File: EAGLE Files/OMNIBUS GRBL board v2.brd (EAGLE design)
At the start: 100.6 x 73.6 mm, 61 parts, among them K1 691131710002, K2 691131710003, K3 691131710003, K4 691131710003, U1 LTV-847S, U2 L7805ACD2T-TR, U3 LM358M/NOPB, U4 LTV-847S, U5 PC817X3NSZ1B, U6 ULN2003AD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

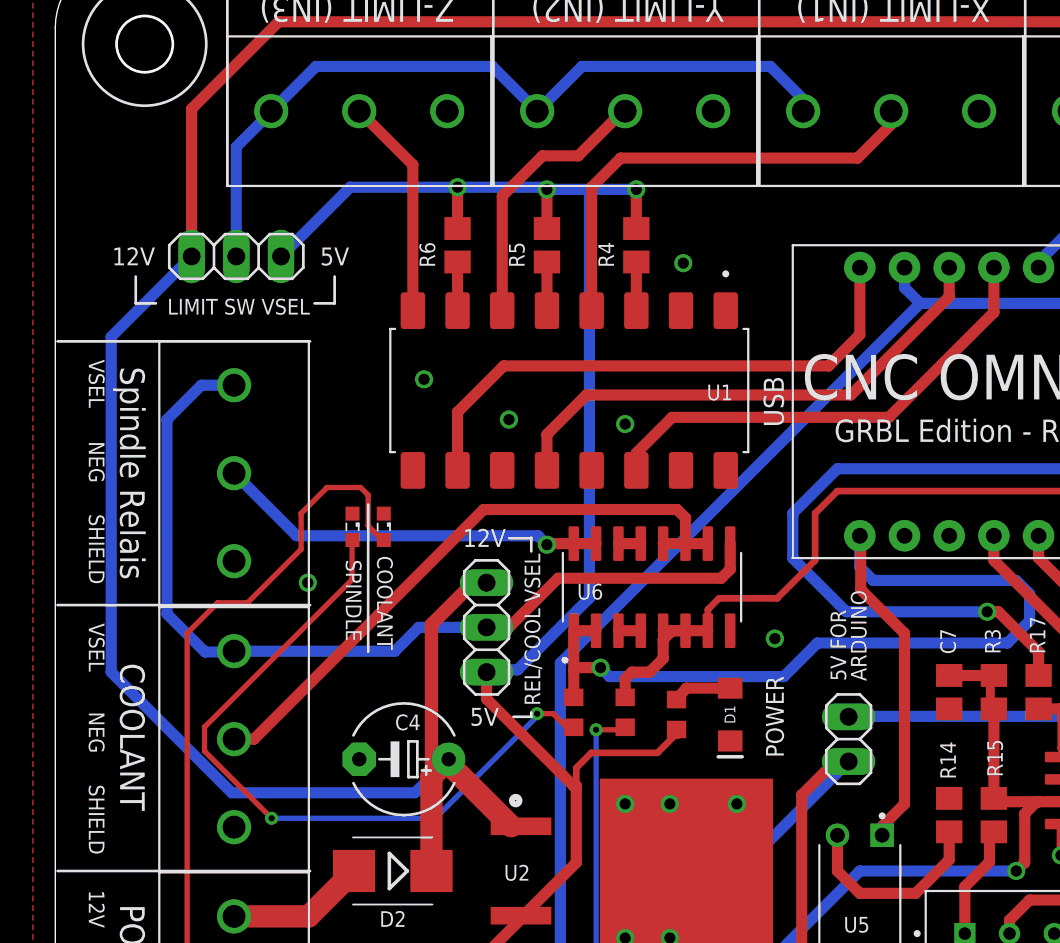
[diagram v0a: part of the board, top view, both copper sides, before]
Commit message: PCB Bugfixes and polishing
• DRV Shield had an routing error (laser indicator LED) also R3 had a wrong value
• New Footprint for the 0.33uF Caps
• Silkscreen polishing
• almost all LEDs are 0805 package now
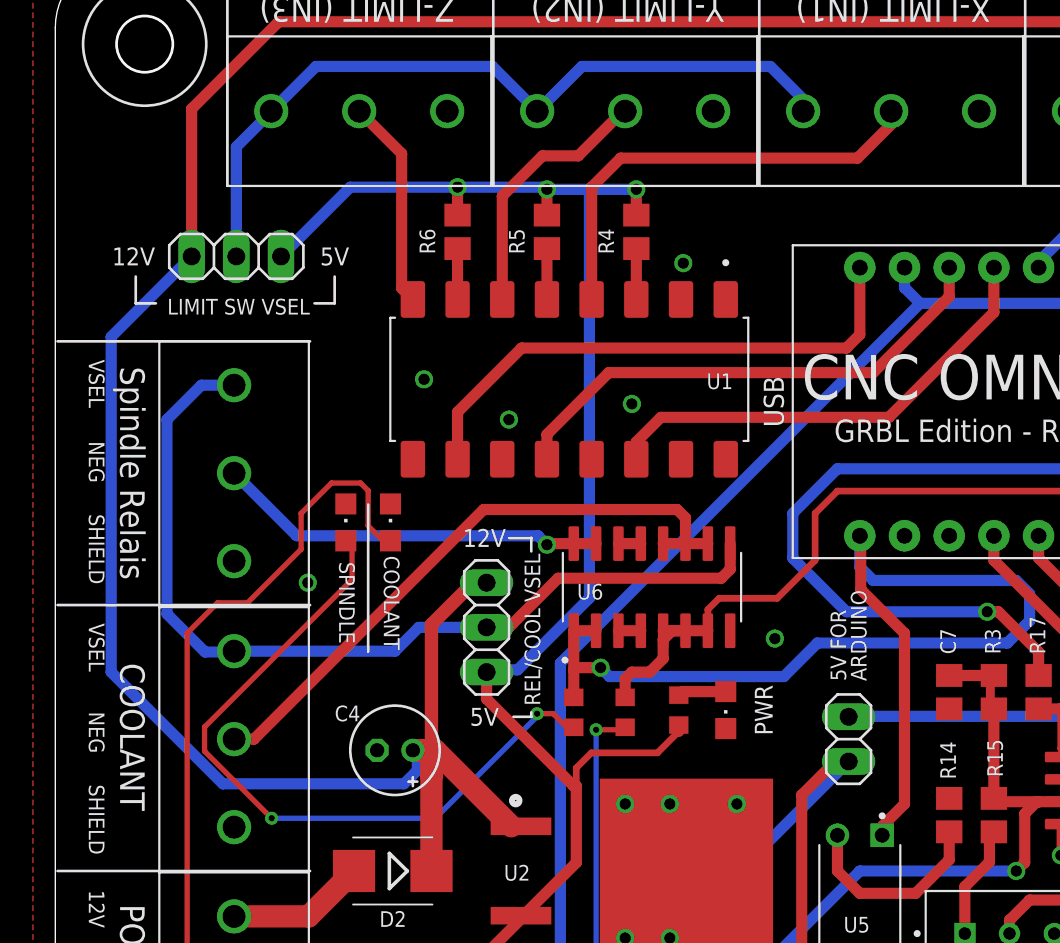
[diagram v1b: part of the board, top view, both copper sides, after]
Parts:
- removed D1: (no value), SparkFun-LED:LED-1206
- removed LED2, LED4: (no value), eagle-ltspice:LED_SML0603
- added GREEN, RED1, RED2: (no value), led:CHIPLED_0805
- C4: value 220uf -> 0.33uF 50V; device rcl:E5-6 -> rcl:E2-5
- moved R4 0.76 mm to (30.5, 56.6)
- moved R5 0.76 mm to (25.4, 56.6)
- moved R6 0.76 mm to (20.3, 56.6)
- moved C4 0.72 mm to (16.8, 27.2)
- moved U1 0.63 mm to (26.7, 48.3)
- moved R2 0.28 mm to (32.9, 29.5)
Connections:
- net GND: now also GREEN.C, RED1.C, RED2.C; no longer D1.C, LED2.C, LED4.C
- net N$1: now also GREEN.A; no longer D1.A
- net N$11: now also RED2.A; no longer LED2.A
- net N$12: now also RED1.A; no longer LED4.A
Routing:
- net 12V: track 255.3 -> 257.3 mm
- net 5V: track 255.9 -> 253.9 mm
- net N$12: track 81.5 -> 82.2 mm
- net INPUT3: track 12.6 -> 12.0 mm
- net INPUT2: track 15.5 -> 14.9 mm
- net INPUT1: track 26.3 -> 25.6 mm
- net IN3: track 31.8 -> 31.2 mm
- net IN2: track 29.8 -> 29.2 mm
- net N$1: track 3.35 -> 2.75 mm
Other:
- board text added: "PWR"

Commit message: Changed voltage regulators
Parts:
- U2: value L7805ACD2T-TR -> MC7805C
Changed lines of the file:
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@@
 <attribute name="PURCHASE-URL" value="https://pricing.snapeda.com/search/part/LTV-847S/?ref=eda" x="13.97" y="6.35" size="1.778" layer="27" rot="R270" display="off"/>
 </element>
-<element name="U2" library="L7805ACD2T-TR" package="TO254P1515X470-3N" value="L7805ACD2T-TR" x="30.226" y="20.32" smashed="yes">
+<element name="U2" library="L7805ACD2T-TR" package="TO254P1515X470-3N" value="MC7805C" x="30.226" y="20.32" smashed="yes">
 <attribute name="AVAILABILITY" value="Good" x="54.356" y="-43.18" size="1.778" layer="27" display="off"/>
 <attribute name="DESCRIPTION" value=" Linear Voltage Regulator IC Positive Fixed 1 Output 1.5A D2PAK " x="54.356" y="-43.18" size="1.778" layer="27" display="off"/>

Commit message: clean up
also added BOM
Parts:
- removed K2, K3: 691131710003, Wurth_Terminal_Blocks_Connectors_rev15d:691131710003
- added CON, RPM: KF301-2P, Wurth_Terminal_Blocks_Connectors_rev15d:691131710002
- BT, JP1: value (none) -> PINHEAD
- DIR1, DIR2, IN4, IN5, IN6, IN7, POW, PWM, VFD: value 691131710002 -> KF301-2P
- IN1, IN2: value 691131710002 -> KF301-3P; device Wurth_Terminal_Blocks_Connectors_rev15d:691131710002 -> Wurth_Terminal_Blocks_Connectors_rev15d:691131710003
- IN3, OUT1, OUT2, STEP: value 691131710003 -> KF301-3P
- RESET: value 22-23-2021 -> JST XH
- moved IN2 56.7 mm to (29.8, 63.5)
- moved IN1 45.9 mm to (45.0, 63.5), turned to 0 degrees
- moved PWM 20.3 mm to (20.3, 7.62), turned to 0 degrees
- renumbered K1 to POW, K4 to IN3, ON_OFF to VFD, ON_OFF1 to DIR1, ON_OFF2 to DIR2, OUT3 to OUT1
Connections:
- net 12V: now also CON.2; no longer IN1.2
- net GND: now also CON.1, IN1.3, IN2.3, RPM.1; no longer IN1.1, IN2.1, K2.3, K3.3
- net INPUT1: now also IN1.2; no longer K2.2
- net INPUT2: now also IN2.2; no longer K3.2
- net IN_VCC: now also IN1.1, IN2.1; no longer K2.1, K3.1
- net PWM_10V: now also RPM.2; no longer PWM.2
- net SPINDLE_PWM: now also PWM.2; no longer IN2.2
